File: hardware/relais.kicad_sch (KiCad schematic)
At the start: 20 parts, among them J4 Mini XLR6, J5 Mini XLR6, J6 Binder 09-0998-00-05, J7 Binder 09-0998-00-05, K1 RT314005, K10 HF49FD_005-1H12T, K11 HF49FD_005-1H12T, K2 HF49FD_005-1H12T, K3 HF49FD_005-1H12T, K4 HF49FD_005-1H12T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

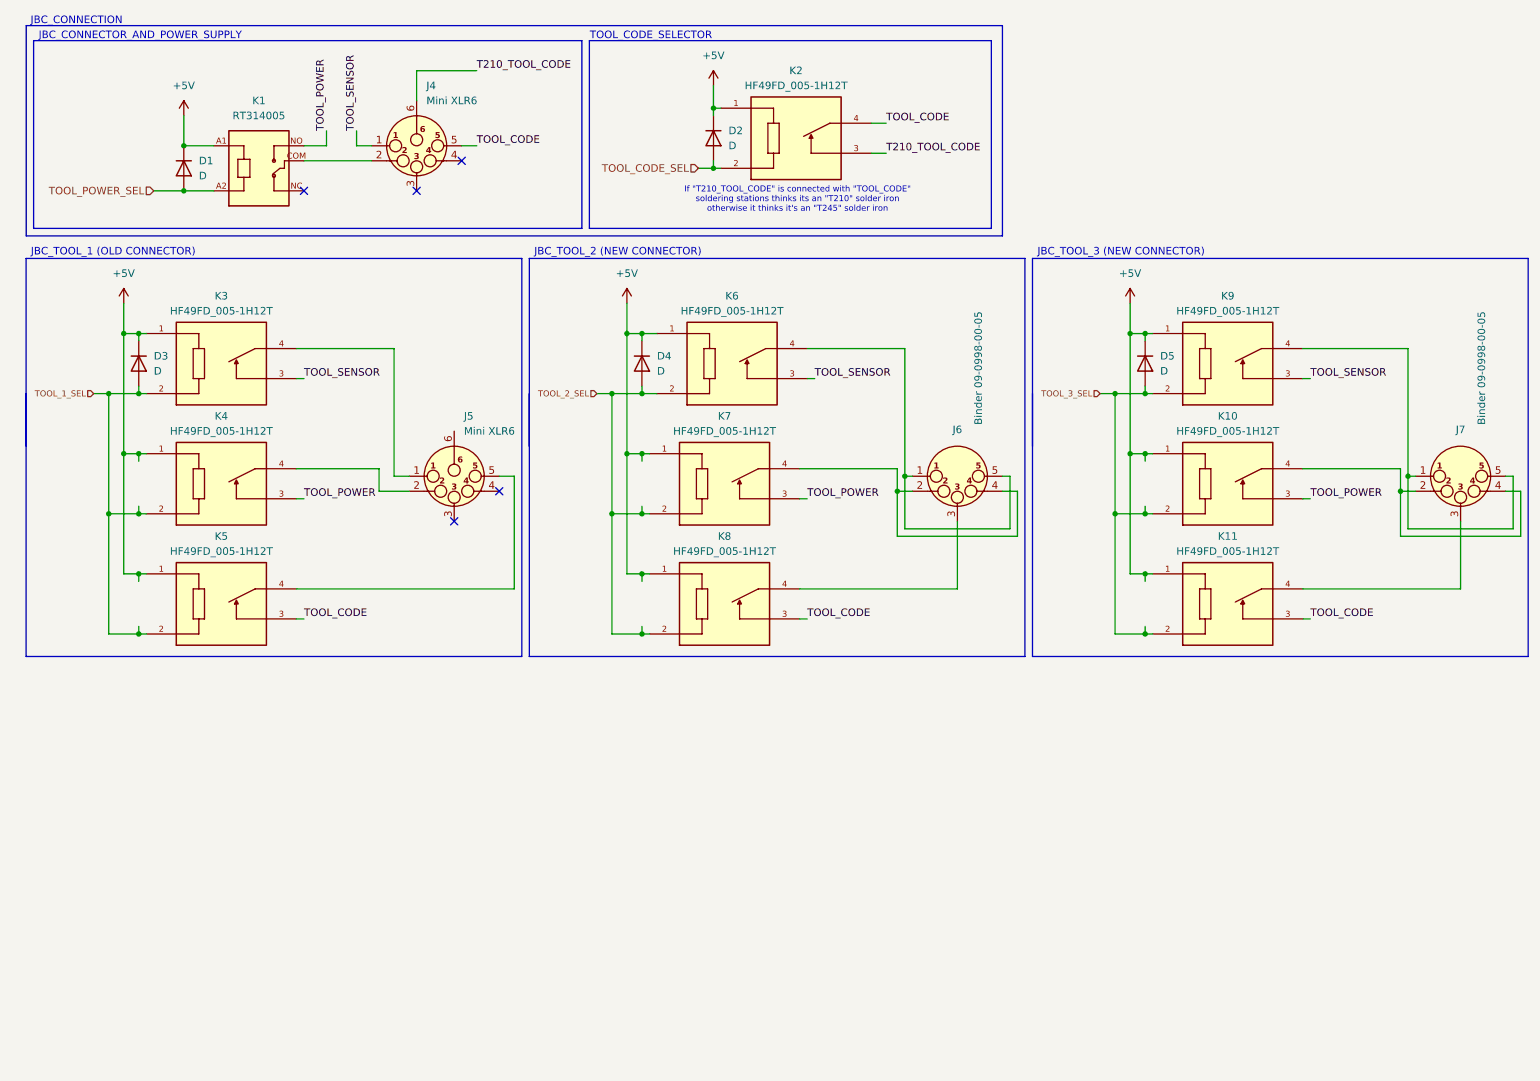
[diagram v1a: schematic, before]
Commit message: added 2.nd "old" jbc connector
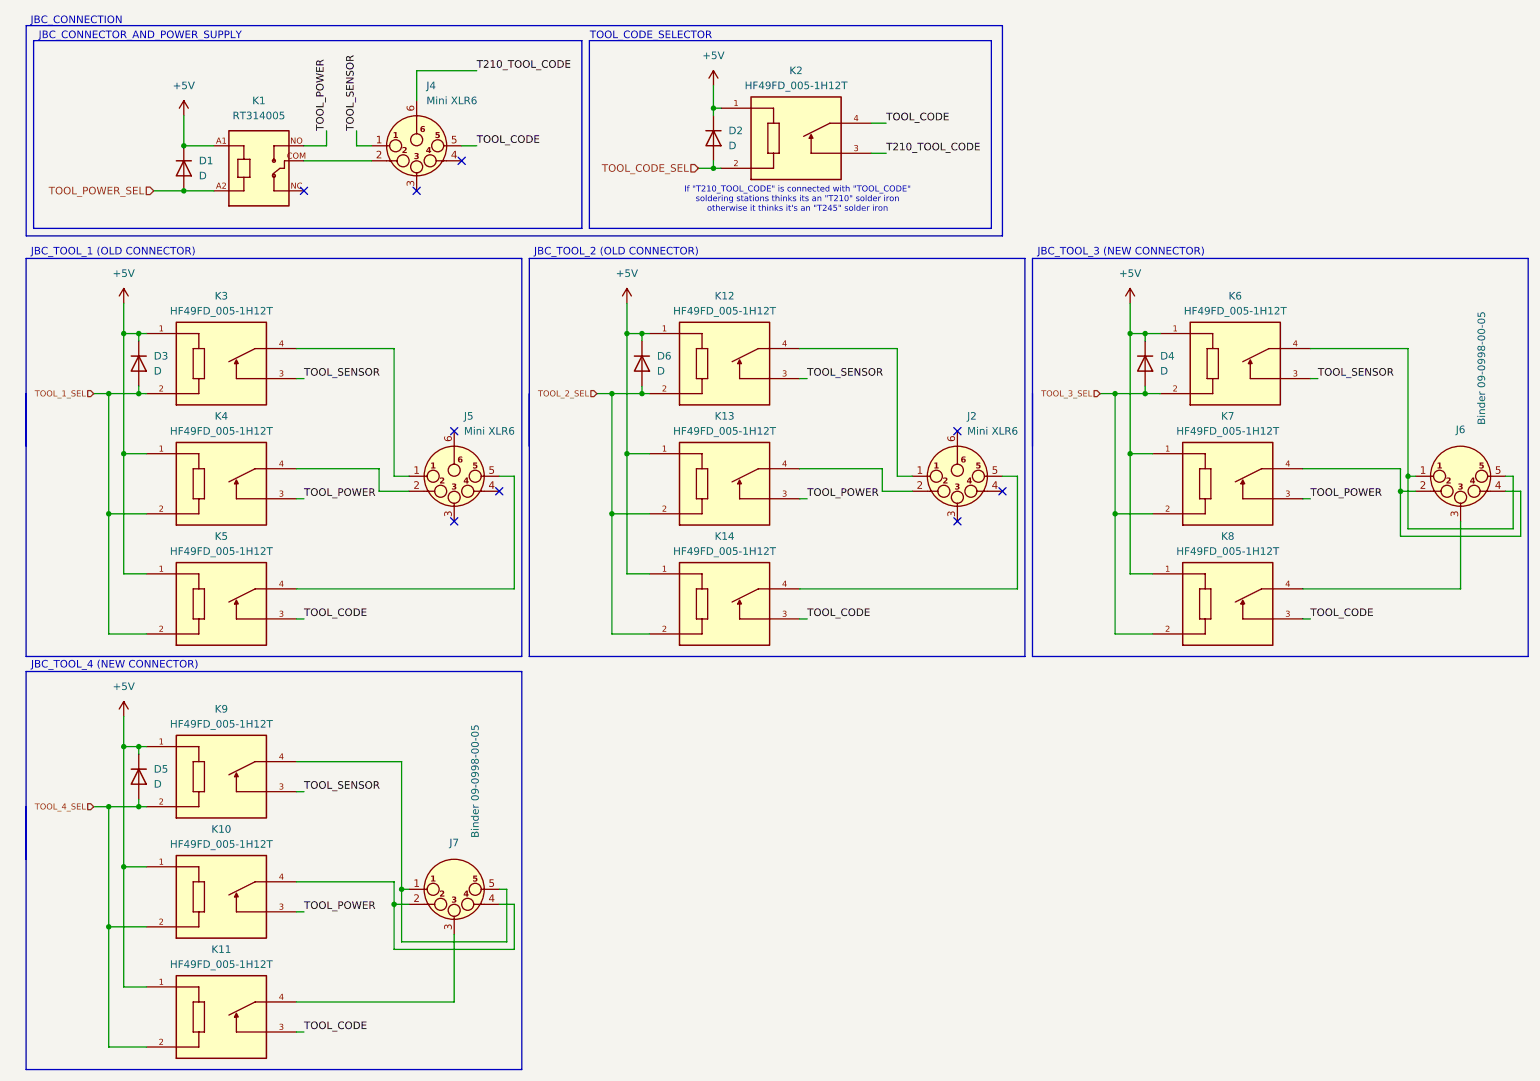
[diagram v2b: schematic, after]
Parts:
- added D6: D, Diode_SMD:D_SOD-123F, symbol Device:D
- added J2: Mini XLR6, Connector_PinHeader_2.54mm:PinHeader_1x03_P2.54mm_Vertical, symbol Connector_Audio:XLR6
- added K12, K13, K14: HF49FD_005-1H12T, HF49FD:HF49FD, symbol HF49FD:HF49FD_005-1H12T
- J4: footprint TerminalBlock_Phoenix:TerminalBlock_Phoenix_MKDS-1,5-4-5.08_1x04_P5.08mm_Horizontal -> Connector_PinHeader_2.54mm:PinHeader_1x04_P2.54mm_Vertical
- J5: footprint TerminalBlock_Phoenix:TerminalBlock_Phoenix_MKDS-1,5-3-5.08_1x03_P5.08mm_Horizontal -> Connector_PinHeader_2.54mm:PinHeader_1x03_P2.54mm_Vertical
- J6, J7: footprint TerminalBlock_Phoenix:TerminalBlock_Phoenix_MKDS-1,5-5-5.08_1x05_P5.08mm_Horizontal -> Connector_PinHeader_2.54mm:PinHeader_1x05_P2.54mm_Vertical
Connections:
- net +5V: now also D6.1 (K), K12.1, K13.1, K14.1
- net TOOL_2_SEL: now also D6.2 (A), K12.2, K13.2, K14.2; no longer D4.2 (A), K6.2, K7.2, K8.2
- net TOOL_3_SEL: now also D4.2 (A), K6.2, K7.2, K8.2; no longer D5.2 (A), K10.2, K11.2, K9.2
- net TOOL_CODE: now also K14.3
- net TOOL_POWER: now also K13.3
- net TOOL_SENSOR: now also K12.3
- new net: J2.1 (P1), K12.4
- new net: J2.2 (P2), K13.4
- new net: J2.5 (P5), K14.4
- new net TOOL_4_SEL: D5.2 (A), K10.2, K11.2, K9.2
- no-connect marks 5 -> 9
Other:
- note added: "JBC_TOOL_2 (OLD CONNECTOR)"
- note added: "JBC_TOOL_4 (NEW CONNECTOR)"
- note removed: "JBC_TOOL_2 (NEW CONNECTOR)"
- moved on the sheet: D4, D5, J6, J7, K10, K11, K6, K7, K8, K9

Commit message: add gerber and bom
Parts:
- J2, J5: Mouser <a href="https://mou.sr/40RtPIA">MKDS 3/ 3-5,08</a> + <a hr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 -> <a href="https://mou.sr/4glJCnv">523-AG6M</a>
- J4: Mouser <a href="https://mou.sr/3CryA2f">MKDS 3/ 4-5,08</a> + <a hr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 -> <a href="https://mou.sr/4glJCnv">523-AG6M</a>
- J6, J7: Mouser <a href="https://mou.sr/40xb1NK">MKDS 3/ 5-5,08</a> + Part 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 -> (none)
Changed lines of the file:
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@@
 			)
 		)
-		(property "Mouser" "<a href=\"https://mou.sr/40RtPIA\">MKDS 3/ 3-5,08</a> + <a href=\"https://mou.sr/3CrlIJy\">523-AG6MCC</a> + <a href=\"https://mou.sr/4glJCnv\">523-AG6M</a>"
+		(property "Mouser" "<a href=\"https://mou.sr/4glJCnv\">523-AG6M</a>"
 			(at 171.45 91.44 0)
 			(effects
@@
 			)
 		)
-		(property "Mouser" "<a href=\"https://mou.sr/3CryA2f\">MKDS 3/ 4-5,08</a> + <a href=\"https://mou.sr/3CrlIJy\">523-AG6MCC</a> + <a href=\"https://mou.sr/4glJCnv\">523-AG6M</a>"
+		(property "Mouser" "<a href=\"https://mou.sr/4glJCnv\">523-AG6M</a>"
 			(at 80.01 35.56 0)
 			(effects
@@
 			)
 		)
-		(property "Mouser" "<a href=\"https://mou.sr/40xb1NK\">MKDS 3/ 5-5,08</a> + Part from RS Components"
+		(property "Mouser" ""
 			(at 86.36 161.29 0)
 			(effects
@@
 			)
 		)
-		(property "Mouser" "<a href=\"https://mou.sr/40RtPIA\">MKDS 3/ 3-5,08</a> + <a href=\"https://mou.sr/3CrlIJy\">523-AG6MCC</a> + <a href=\"https://mou.sr/4glJCnv\">523-AG6M</a>"
+		(property "Mouser" "<a href=\"https://mou.sr/4glJCnv\">523-AG6M</a>"
 			(at 86.36 91.44 0)
 			(effects
@@
 			)
 		)
-		(property "Mouser" "<a href=\"https://mou.sr/40xb1NK\">MKDS 3/ 5-5,08</a> + Part from RS Components"
+		(property "Mouser" ""
 			(at 256.54 91.44 0)
 			(effects
